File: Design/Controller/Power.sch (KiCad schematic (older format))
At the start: 17 parts, among them Q1 IRF644, U3 LM2576, U4 MAX1771

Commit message: Add part numbers to symbols in NixieController schematic for BOM
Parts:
- C1, C2: Digikey # (none) -> PCE3898DKR-ND; Manufacturer (none) -> PANASONIC
- C3: Digikey # (none) -> 478-TPSD107M020R0150DKR-ND; Manufacturer (none) -> AVX
- C4, C5: Digikey # (none) -> 1276-1007-6-ND; Manufacturer (none) -> SAMSUNG
- C6: Digikey # (none) -> PCE3432DKR-ND; Manufacturer (none) -> PANASONIC
- D1: Digikey # (none) -> 1N5822-E3/54GITR-ND; Manufacturer (none) -> VISHAY
- D2: Digikey # (none) -> ES2F-E3/52TGIDKR-ND; Manufacturer (none) -> VISHAY
- L1, L2: Digikey # (none) -> 513-1526-6-ND; Manufacturer (none) -> EATON
- Q1: Digikey # (none) -> IRF644STRLPBFDKR-ND; Manufacturer (none) -> VISHAY
- R3: Digikey # (none) -> YAG2156DKR-ND; Manufacturer (none) -> YAGEO
- R4: Digikey # (none) -> 311-1.2MERDKR-ND; Manufacturer (none) -> YAGEO
- R5: Digikey # (none) -> 311-10KARDKR-ND; Manufacturer (none) -> YAGEO
- RV1: Digikey # (none) -> 3362P-502LF-ND; Manufacturer (none) -> BOURNS
- U3: Digikey # (none) -> LM2576SX-5.0/NOPBDKR-ND; Manufacturer (none) -> TI
- U4: Digikey # (none) -> MAX1771CSA+DKR-ND; Manufacturer (none) -> MAXIM
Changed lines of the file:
@@
 F 1 "MAX1771" H 7300 3950 50  0000 C CNN
 F 2 "Package_SO:SOIC-8_3.9x4.9mm_P1.27mm" H 7000 4600 50  0001 C CNN
-F 3 "" H 7000 4600 50  0001 C CNN
+F 3 "MAX1771CSA+T" H 7000 4600 50  0001 C CNN
+F 4 "MAX1771CSA+DKR-ND" H 7000 3600 50  0001 C CNN "Digikey #"
+F 5 "MAXIM" H 7000 3600 50  0001 C CNN "Manufacturer"
 	1    7000 3600
 	1    0    0    -1
@@
 F 1 "100nF" H 6415 4005 50  0000 L CNN
 F 2 "Capacitor_SMD:C_0805_2012Metric" H 6338 3900 50  0001 C CNN
-F 3 "~" H 6300 4050 50  0001 C CNN
+F 3 "CL21F104ZBCNNNC" H 6300 4050 50  0001 C CNN
+F 4 "1276-1007-6-ND" H 6300 4050 50  0001 C CNN "Digikey #"
+F 5 "SAMSUNG" H 6300 4050 50  0001 C CNN "Manufacturer"
 	1    6300 4050
 	1    0    0    -1
@@
 F 1 "IRF644" H 8006 3355 50  0000 L CNN
 F 2 "Package_TO_SOT_SMD:TO-263-2" H 8000 3500 50  0001 C CNN
-F 3 "~" H 7800 3400 50  0001 C CNN
+F 3 "IRF644STRLPBF" H 7800 3400 50  0001 C CNN
+F 4 "IRF644STRLPBFDKR-ND" H 7800 3400 50  0001 C CNN "Digikey #"
+F 5 "VISHAY" H 7800 3400 50  0001 C CNN "Manufacturer"
 	1    7800 3400
 	1    0    0    -1
@@
 F 1 "100uH,2A" V 7749 3100 50  0000 C CNN
 F 2 "Inductor_SMD:L_12x12mm_H4.5mm" H 7650 3100 50  0001 C CNN
-F 3 "~" H 7650 3100 50  0001 C CNN
+F 3 "DR125-101-R" H 7650 3100 50  0001 C CNN
+F 4 "513-1526-6-ND" H 7650 3100 50  0001 C CNN "Digikey #"
+F 5 "EATON" H 7650 3100 50  0001 C CNN "Manufacturer"
 	1    7650 3100
 	0    -1   -1   0
@@
 F 1 "0.05,1W" H 7970 4005 50  0000 L CNN
 F 2 "Resistor_SMD:R_2512_6332Metric" V 7830 4050 50  0001 C CNN
-F 3 "~" H 7900 4050 50  0001 C CNN
+F 3 "PE2512FKE070R05L" H 7900 4050 50  0001 C CNN
+F 4 "YAG2156DKR-ND" H 7900 4050 50  0001 C CNN "Digikey #"
+F 5 "YAGEO" H 7900 4050 50  0001 C CNN "Manufacturer"
 	1    7900 4050
 	1    0    0    -1
@@
 F 2 "Diode_SMD:D_SMB" H 8250 3100 50  0001 C CNN
 F 3 "ES2F-E3/52T" H 8250 3100 50  0001 C CNN
+F 4 "ES2F-E3/52TGIDKR-ND" H 8250 3100 50  0001 C CNN "Digikey #"
+F 5 "VISHAY" H 8250 3100 50  0001 C CNN "Manufacturer"
 	1    8250 3100
 	-1   0    0    1
@@
 F 1 "100nF" H 6315 3255 50  0000 L CNN
 F 2 "Capacitor_SMD:C_0805_2012Metric" H 6238 3150 50  0001 C CNN
-F 3 "~" H 6200 3300 50  0001 C CNN
+F 3 "CL21F104ZBCNNNC" H 6200 3300 50  0001 C CNN
+F 4 "1276-1007-6-ND" H 6200 3300 50  0001 C CNN "Digikey #"
+F 5 "SAMSUNG" H 6200 3300 50  0001 C CNN "Manufacturer"
 	1    6200 3300
 	1    0    0    -1
@@
 F 1 "1M2,250V" H 8720 3505 50  0000 L CNN
 F 2 "Resistor_SMD:R_1206_3216Metric" V 8580 3550 50  0001 C CNN
-F 3 "~" H 8650 3550 50  0001 C CNN
+F 3 "RC1206JR-071M2L" H 8650 3550 50  0001 C CNN
+F 4 "311-1.2MERDKR-ND" H 8650 3550 50  0001 C CNN "Digikey #"
+F 5 "YAGEO" H 8650 3550 50  0001 C CNN "Manufacturer"
 	1    8650 3550
 	1    0    0    -1
@@
 F 1 "10K" H 8720 4005 50  0000 L CNN
 F 2 "Resistor_SMD:R_0805_2012Metric" V 8580 4050 50  0001 C CNN
-F 3 "~" H 8650 4050 50  0001 C CNN
+F 3 "RC0805JR-0710KL" H 8650 4050 50  0001 C CNN
+F 4 "311-10KARDKR-ND" H 8650 4050 50  0001 C CNN "Digikey #"
+F 5 "YAGEO" H 8650 4050 50  0001 C CNN "Manufacturer"
 	1    8650 4050
 	1    0    0    -1
@@
 F 2 "Capacitor_SMD:CP_Elec_10x10" H 9288 3400 50  0001 C CNN
 F 3 "EEV-EB2E100Q" H 9250 3550 50  0001 C CNN
+F 4 "PCE3432DKR-ND" H 9250 3550 50  0001 C CNN "Digikey #"
+F 5 "PANASONIC" H 9250 3550 50  0001 C CNN "Manufacturer"
 	1    9250 3550
 	1    0    0    -1
@@
 F 1 "100uF,Low ESR" H 5468 3255 50  0000 L CNN
 F 2 "Capacitor_Tantalum_SMD:CP_EIA-7343-31_Kemet-D" H 5388 3150 50  0001 C CNN
-F 3 "TPSD107M020R0085" H 5350 3300 50  0001 C CNN
+F 3 "TPSD107M020R0150" H 5350 3300 50  0001 C CNN
+F 4 "478-TPSD107M020R0150DKR-ND" H 5350 3300 50  0001 C CNN "Digikey #"
+F 5 "AVX" H 5350 3300 50  0001 C CNN "Manufacturer"
 	1    5350 3300
 	1    0    0    -1
@@
 F 1 "10K" V 8444 4350 50  0000 C CNN
 F 2 "Potentiometer_THT:Potentiometer_Bourns_3339P_Vertical" H 8650 4350 50  0001 C CNN
-F 3 "~" H 8650 4350 50  0001 C CNN
+F 3 "3362P-1-502LF" H 8650 4350 50  0001 C CNN
+F 4 "3362P-502LF-ND" H 8650 4350 50  0001 C CNN "Digikey #"
+F 5 "BOURNS" H 8650 4350 50  0001 C CNN "Manufacturer"
 	1    8650 4350
 	0    -1   -1   0
@@
 F 1 "LM2576" H 2600 3574 50  0000 C CNN
 F 2 "Package_TO_SOT_SMD:TO-263-5_TabPin3" H 2600 3700 50  0001 C CNN
-F 3 "" H 2600 3700 50  0001 C CNN
+F 3 "LM2576SX-5.0/NOPB" H 2600 3700 50  0001 C CNN
+F 4 "LM2576SX-5.0/NOPBDKR-ND" H 2600 3300 50  0001 C CNN "Digikey #"
+F 5 "TI" H 2600 3300 50  0001 C CNN "Manufacturer"
 	1    2600 3300
 	1    0    0    -1
@@
 F 1 "100uF" H 1918 3355 50  0000 L CNN
 F 2 "Capacitor_SMD:CP_Elec_6.3x7.7" H 1838 3250 50  0001 C CNN
-F 3 "TPSD107M020R0085" H 1800 3400 50  0001 C CNN
+F 3 "EEE-1EA101XP" H 1800 3400 50  0001 C CNN
+F 4 "PCE3898DKR-ND" H 1800 3400 50  0001 C CNN "Digikey #"
+F 5 "PANASONIC" H 1800 3400 50  0001 C CNN "Manufacturer"
 	1    1800 3400
 	1    0    0    -1
@@
 F 1 "IN5822" V 3195 3679 50  0000 L CNN
 F 2 "Diode_THT:D_DO-201AD_P12.70mm_Horizontal" H 3150 3600 50  0001 C CNN
-F 3 "~" H 3150 3600 50  0001 C CNN
+F 3 "1N5822-E3/54" H 3150 3600 50  0001 C CNN
+F 4 "1N5822-E3/54GITR-ND" H 3150 3600 50  0001 C CNN "Digikey #"
+F 5 "VISHAY" H 3150 3600 50  0001 C CNN "Manufacturer"
 	1    3150 3600
 	0    1    1    0
@@
 F 1 "100uH,2A" V 3450 3400 50  0000 C CNN
 F 2 "Inductor_SMD:L_12x12mm_H4.5mm" H 3350 3400 50  0001 C CNN
-F 3 "~" H 3350 3400 50  0001 C CNN
+F 3 "DR125-101-R" H 3350 3400 50  0001 C CNN
+F 4 "513-1526-6-ND" H 3350 3400 50  0001 C CNN "Digikey #"
+F 5 "EATON" H 3350 3400 50  0001 C CNN "Manufacturer"
 	1    3350 3400
 	0    -1   -1   0
@@
 F 1 "100uF" H 3768 3555 50  0000 L CNN
 F 2 "Capacitor_SMD:CP_Elec_6.3x7.7" H 3688 3450 50  0001 C CNN
-F 3 "TPSD107M020R0085" H 3650 3600 50  0001 C CNN
+F 3 "EEE-1EA101XP" H 3650 3600 50  0001 C CNN
+F 4 "PCE3898DKR-ND" H 3650 3600 50  0001 C CNN "Digikey #"
+F 5 "PANASONIC" H 3650 3600 50  0001 C CNN "Manufacturer"
 	1    3650 3600
 	1    0    0    -1

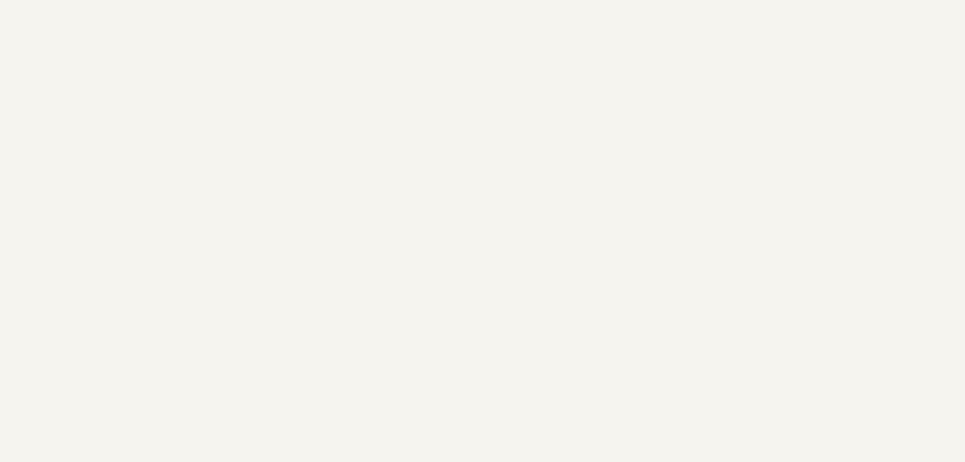
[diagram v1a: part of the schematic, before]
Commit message: Add license notice to all human readable files
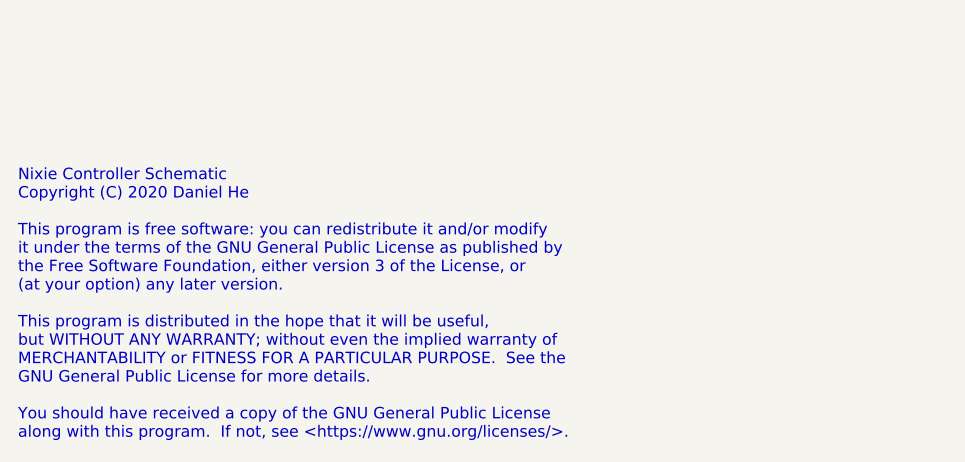
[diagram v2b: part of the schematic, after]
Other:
- note added: "Nixie Controller Schematic\nCopyright (C) 2020 Daniel He\n\nThis program is free software: you can redistribute it and/or modify\nit under the terms of the GNU General Public License as published by\nthe Free Software Foundation, either version 3 of the License, or\n(at your option) any later version.\n\nThis program is distributed in the hope that it will be useful,\nbut WITHOUT ANY WARRANTY; wi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"
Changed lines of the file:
@@
 Wire Wire Line
 	9250 3100 9250 3400
+Text Notes 550  7700 0    50   ~ 0
+Nixie Controller Schematic\nCopyright (C) 2020 Daniel He\n\nThis program is free software: you can redistribute it and/or modify\nit under the terms of the GNU General Public License as published by\nthe Free Software Foundation, either version 3 of the License, or\n(at your option) any later version.\n\nThis program is distributed in the hope that it will be useful,\nbut WITHOUT ANY WARRANTY; without even the implied warranty of\nMERCHANTABILITY or FITNESS FOR A PARTICULAR PURPOSE.  See the\nGNU General Public License for more details.\n\nYou should have received a copy of the GNU General Public License\nalong with this program.  If not, see <https://www.gnu.org/licenses/>.
 $EndSCHEMATC
